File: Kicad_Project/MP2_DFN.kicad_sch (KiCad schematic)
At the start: 228 parts, among them J1 Conn_01x07, J2 Conn_01x06, J3 Conn_01x06, J4 Conn_01x06, SW1 Conn_01x02, U1 NCP5183 / TF2190-TAH, U2 NCP5183 / TF2190-TAH, U3 NCP5183 / TF2190-TAH, U4 NCS20034DR2G, U5 STM32F401CCU6_Balckpill, U6 PQDE6W-Q110 / RD5-110S12W, U7 12_DCDC_5

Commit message: changed all file names
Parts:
- QA1, QA2, QA3, QA4, QA5, QA6, QB1, QB2, QB3, QB4, QB5, QB6, QC1, QC2, QC3, QC4, QC5, QC6: symbol CCC_ESC_Custom_Symbols:MDP10N027 -> MP2_DFN_Custom_Symbols:MDP10N027
- SHA1, SHA2, SHA3, SHB1, SHB2, SHB3, SHC1, SHC2, SHC3: footprint CCC_ESC_Custom_parts:Shunt_2512_6332Metric -> MP2_DFN_Custom_parts:Shunt_2512_6332Metric
- U1, U2, U3: symbol CCC_ESC_Custom_Symbols:NCP5183 -> MP2_DFN_Custom_Symbols:NCP5183
- U5: footprint CCC_ESC_Custom_parts:Blackpill_STM32F401CEU6 -> MP2_DFN_Custom_parts:Blackpill_STM32F401CEU6; symbol CCC_ESC_Custom_Symbols:STM32F401CCU6_Balckpill -> MP2_DFN_Custom_Symbols:STM32F401CCU6_Balckpill
- U6: footprint CCC_ESC_Custom_parts:PQDE6W -> MP2_DFN_Custom_parts:PQDE6W; symbol CCC_ESC_Custom_Symbols:PQDE6W-Q110 -> MP2_DFN_Custom_Symbols:PQDE6W-Q110
- U7: footprint CCC_ESC_Custom_parts:12_DCDC_5 -> MP2_DFN_Custom_parts:12_DCDC_5; symbol CCC_ESC_Custom_Symbols:TO220_replacement_module -> MP2_DFN_Custom_Symbols:TO220_replacement_module

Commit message: created manufacturing files
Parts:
- removed SW1: Conn_01x02, Resistor_SMD:R_1206_3216Metric_Pad1.30x1.75mm_HandSolder, symbol Connector_Generic:Conn_01x02
- CR1, CR2, CR3, CR4, CR5, CS1, CS2, CS3, D10, D8, J1, J2, J3, J4, JP1, JP2, JP3, NT1, NT2, NT3, NT4, NT5, NT6, NTC1, PHA_1, PHA_2, PHB_1, PHB_2, PHC_1, PHC_2, QA1, QA2, QA3, QA4, QA5, QA6, QB1, QB2, QB3, QB4, QB5, QB6, QC1, QC2, QC3, QC4, QC5, QC6, RS1, RS2, RS3, Tp12V1, TpGND1, TpGND2, TpGND3, TpGND4, TpGS2, TpGS4, TpGS6, U5, U6, U7: now left out of the parts list
- R38, R40: value 47k -> 13k; LCSC C25819 -> C22797
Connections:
- net at C5.1, D7.1 (A1), D8.1 (A1)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: now also R1.1, R2.1
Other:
- note added: "R38 and R40 values for Vsense dividers - for different power stage Voltages. Since the we're going with the NVMTSC4D3N15MC MOSFETs, Vsense will be for 150V: 150V max 30s lipo, overvoltage cutoff at 137V) - 13k (LCSC C22797) 100V max 20s lipo, overvoltage cutoff at 92.6V) - 47k (LCSC C25819) 80V max 16s lipo, overvoltage cutoff at 75.6V) - Do not fit at all!"
- note removed: "CAUTION WITH ORDERING -- FIX BOM FOR 150V VSENSE"
- note removed: "R38 and R40 values for Vsense dividers - for different power stage Voltages. 80V power stage (max 16s lipo, overvoltage cutoff at 75.6V) - Do not fit at all! 100V power stage (max 20s lipo, overvoltage cutoff at 92.6V) - 47k (LCSC C25819) 150V power stage (max 30s lipo, overvoltage cutoff at 137V) - 13k (LCSC C22797)"
- moved on the sheet: R1, R2

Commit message: order sent to jlcpcb
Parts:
- U1, U2, U3: value NCP5183 / TF2190-TAH -> TF2190-TAH
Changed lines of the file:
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@@
       (effects (font (size 1.27 1.27)))
     )
-    (property "Value" "NCP5183 / TF2190-TAH" (at 431.165 228.6 0)
+    (property "Value" "TF2190-TAH" (at 431.165 228.6 0)
       (effects (font (size 1.27 1.27)))
     )
@@
       (effects (font (size 1.27 1.27)) hide)
     )
-    (property "Value" "NCP5183 / TF2190-TAH" (at 431.165 67.31 0)
+    (property "Value" "TF2190-TAH" (at 431.165 67.31 0)
       (effects (font (size 1.27 1.27)))
     )
@@
       (effects (font (size 1.27 1.27)))
     )
-    (property "Value" "NCP5183 / TF2190-TAH" (at 431.165 147.32 0)
+    (property "Value" "TF2190-TAH" (at 431.165 147.32 0)
       (effects (font (size 1.27 1.27)))
     )

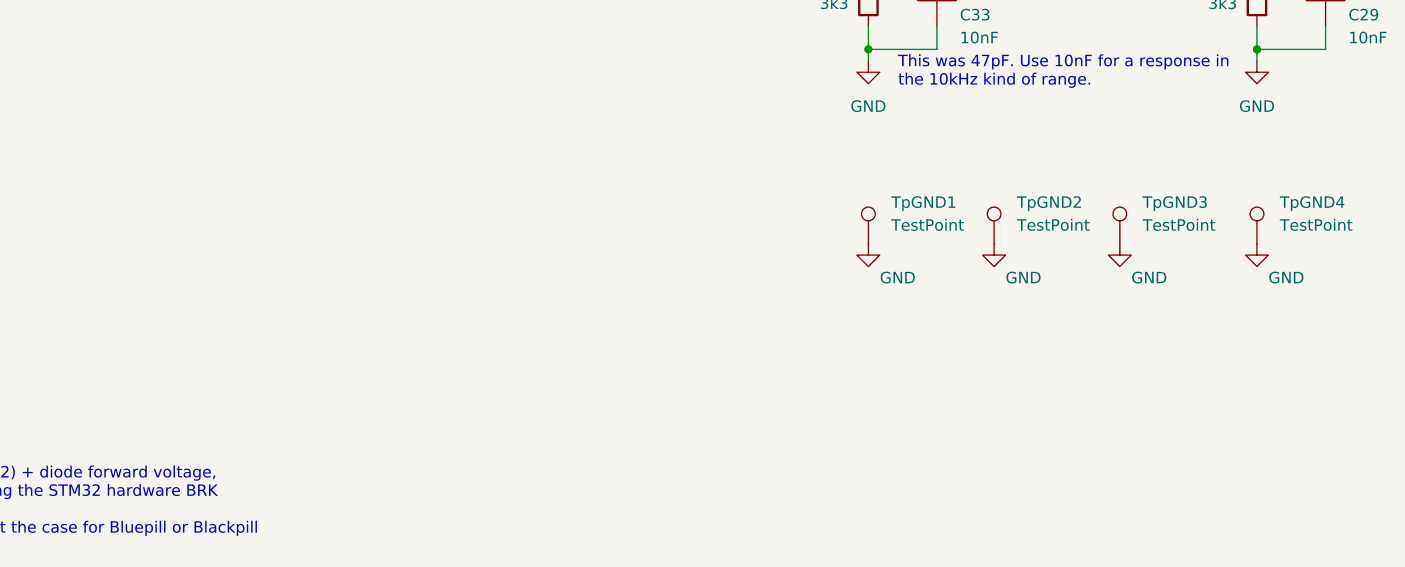
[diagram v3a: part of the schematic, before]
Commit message: fixed GND breaks, increased bus bars
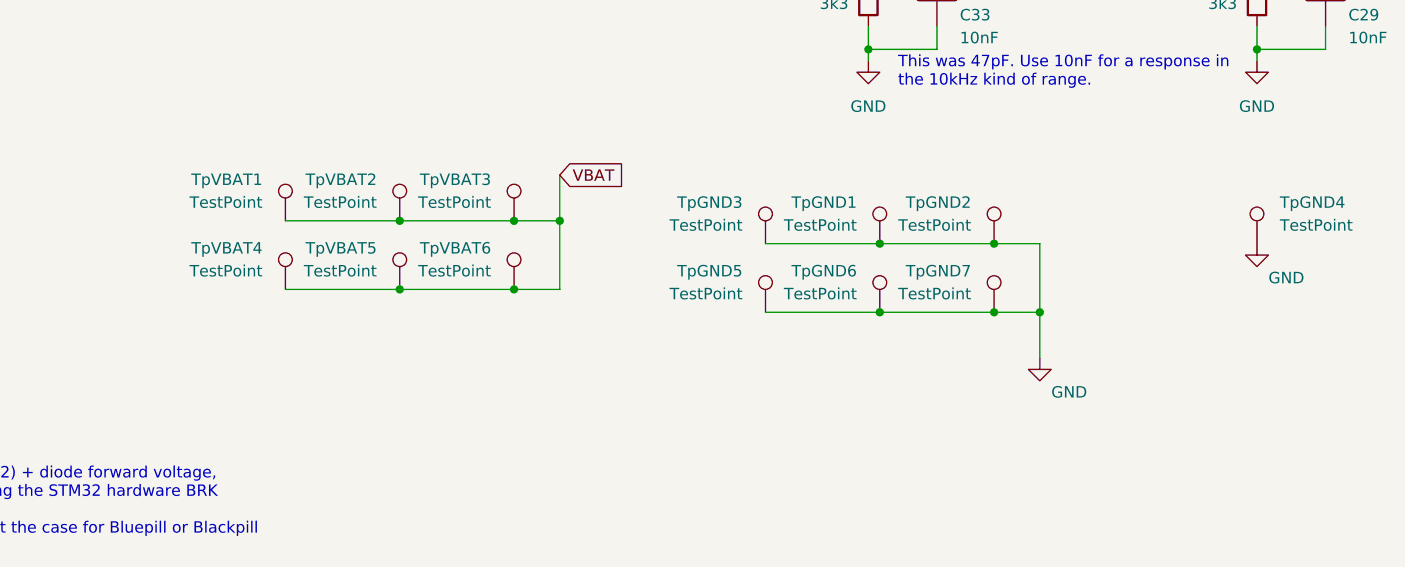
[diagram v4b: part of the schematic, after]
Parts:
- added TpGND5, TpGND6, TpGND7, TpVBAT1, TpVBAT2, TpVBAT3, TpVBAT4, TpVBAT5, TpVBAT6: TestPoint, Busbars:my_testpoint_D1.7mm, symbol Connector:TestPoint
- TpGND1, TpGND2, TpGND3: footprint TestPoint:TestPoint_THTPad_D2.0mm_Drill1.0mm -> Busbars:my_testpoint_D1.7mm
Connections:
- net GND: now also TpGND5.1, TpGND6.1, TpGND7.1
- net VBAT: now also TpVBAT1.1, TpVBAT2.1, TpVBAT3.1, TpVBAT4.1, TpVBAT5.1, TpVBAT6.1
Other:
- moved on the sheet: TpGND3

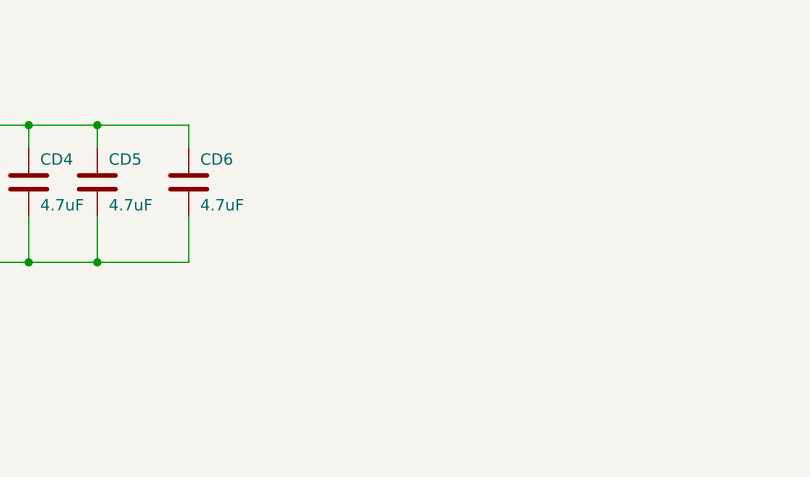
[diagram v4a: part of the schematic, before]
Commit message: added caps, prettied up phase connectors
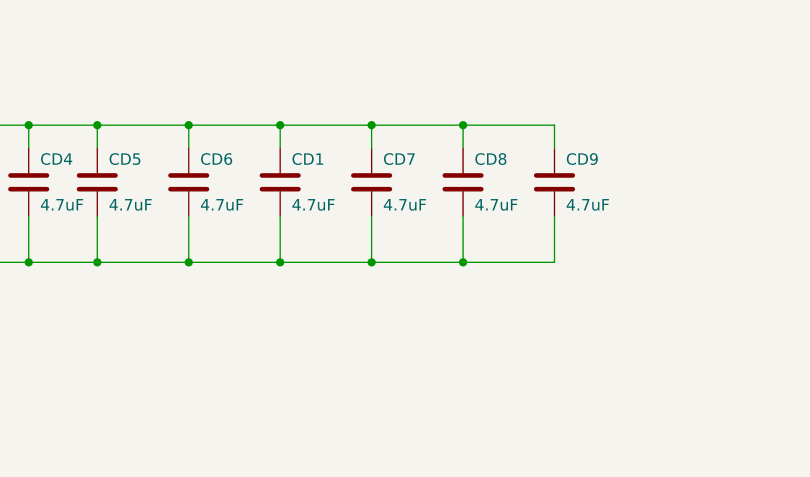
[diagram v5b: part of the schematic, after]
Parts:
- added CD1, CD7, CD8, CD9: 4.7uF, Capacitor_SMD:C_1210_3225Metric, symbol Device:C
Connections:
- net GND: now also CD1.2, CD7.2, CD8.2, CD9.2
- net VBAT: now also CD1.1, CD7.1, CD8.1, CD9.1
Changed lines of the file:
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@@
   (junction (at 486.41 156.21) (diameter 0) (color 0 0 0 0)
   )
+  (junction (at 179.705 43.815) (diameter 0) (color 0 0 0 0)
+  )
   (junction (at 452.755 76.2) (diameter 0) (color 0 0 0 0)
   )
@@
   (junction (at 250.698 380.492) (diameter 0) (color 0 0 0 0)
   )
+  (junction (at 149.225 43.815) (diameter 0) (color 0 0 0 0)
+  )
   (junction (at 448.31 241.3) (diameter 0) (color 0 0 0 0)
   )
@@
   (junction (at 491.49 328.93) (diameter 0) (color 0 0 0 0)
   )
+  (junction (at 159.385 43.815) (diameter 0) (color 0 0 0 0)
+  )
   (junction (at 534.67 241.3) (diameter 0) (color 0 0 0 0)
   )
@@
   (junction (at 443.23 59.69) (diameter 0) (color 0 0 0 0)
   )
+  (junction (at 179.705 28.575) (diameter 0) (color 0 0 0 0)
+  )
   (junction (at 538.48 80.01) (diameter 0) (color 0 0 0 0)
   )
@@
   (junction (at 246.38 46.99) (diameter 0) (color 0 0 0 0)
   )
+  (junction (at 169.545 43.815) (diameter 0) (color 0 0 0 0)
+  )
   (junction (at 451.485 241.3) (diameter 0) (color 0 0 0 0)
   )
@@
   (junction (at 466.725 229.87) (diameter 0) (color 0 0 0 0)
   )
+  (junction (at 169.545 28.575) (diameter 0) (color 0 0 0 0)
+  )
   (junction (at 474.98 180.975) (diameter 0) (color 0 0 0 0)
   )
@@
   (junction (at 526.415 229.87) (diameter 0) (color 0 0 0 0)
   )
+  (junction (at 149.225 28.575) (diameter 0) (color 0 0 0 0)
+  )
   (junction (at 419.1 256.54) (diameter 0) (color 0 0 0 0)
   )
@@
   (junction (at 140.97 133.35) (diameter 0) (color 0 0 0 0)
   )
+  (junction (at 159.385 28.575) (diameter 0) (color 0 0 0 0)
+  )
   (junction (at 406.4 360.68) (diameter 0) (color 0 0 0 0)
   )
@@
     (stroke (width 0) (type default))
   )
+  (wire (pts (xy 149.225 43.815) (xy 159.385 43.815))
+    (stroke (width 0) (type default))
+  )
   (wire (pts (xy 487.68 160.02) (xy 504.19 160.02))
     (stroke (width 0) (type default))
@@
     (stroke (width 0) (type default))
   )
+  (wire (pts (xy 159.385 43.815) (xy 169.545 43.815))
+    (stroke (width 0) (type default))
+  )
+  (wire (pts (xy 159.385 28.575) (xy 159.385 31.115))
+    (stroke (width 0) (type default))
+  )
   (wire (pts (xy 458.47 72.39) (xy 458.47 80.01))
     (stroke (width 0) (type default))
@@
     (stroke (width 0) (type default))
   )
+  (wire (pts (xy 179.705 43.815) (xy 189.865 43.815))
+    (stroke (width 0) (type default))
+  )
   (wire (pts (xy 86.36 63.5) (xy 86.36 67.31))
     (stroke (width 0) (type default))
@@
     (stroke (width 0) (type default))
   )
+  (wire (pts (xy 179.705 38.735) (xy 179.705 43.815))
+    (stroke (width 0) (type default))
+  )
   (wire (pts (xy 243.84 33.02) (xy 246.38 33.02))
     (stroke (width 0) (type default))
@@
     (stroke (width 0) (type default))
   )
+  (wire (pts (xy 179.705 28.575) (xy 189.865 28.575))
+    (stroke (width 0) (type default))
+  )
   (wire (pts (xy 104.14 241.3) (xy 110.49 241.3))
     (stroke (width 0) (type default))
@@
     (stroke (width 0) (type default))
   )
+  (wire (pts (xy 169.545 43.815) (xy 179.705 43.815))
+    (stroke (width 0) (type default))
+  )
   (wire (pts (xy 466.09 148.59) (xy 466.725 148.59))
     (stroke (width 0) (type default))
@@
     (stroke (width 0) (type default))
   )
+  (wire (pts (xy 189.865 38.735) (xy 189.865 43.815))
+    (stroke (width 0) (type default))
+  )
   (wire (pts (xy 448.31 160.02) (xy 448.31 176.53))
     (stroke (width 0) (type default))
@@
     (stroke (width 0) (type default))
   )
+  (wire (pts (xy 169.545 28.575) (xy 169.545 31.115))
+    (stroke (width 0) (type default))
+  )
   (wire (pts (xy 60.96 119.38) (xy 60.96 121.92))
     (stroke (width 0) (type default))
@@
     (stroke (width 0) (type default))
   )
+  (wire (pts (xy 179.705 28.575) (xy 179.705 31.115))
+    (stroke (width 0) (type default))
+  )
   (wire (pts (xy 504.19 140.97) (xy 504.19 143.51))
     (stroke (width 0) (type default))
@@
     (stroke (width 0) (type default))
   )
+  (wire (pts (xy 159.385 28.575) (xy 169.545 28.575))
+    (stroke (width 0) (type default))
+  )
   (wire (pts (xy 518.795 152.4) (xy 518.16 152.4))
     (stroke (width 0) (type default))
@@
     (stroke (width 0) (type default))
   )
+  (wire (pts (xy 149.225 28.575) (xy 159.385 28.575))
+    (stroke (width 0) (type default))
+  )
   (wire (pts (xy 156.718 141.732) (xy 156.718 144.272))
     (stroke (width 0) (type default))
@@
     (stroke (width 0) (type default))
   )
+  (wire (pts (xy 169.545 28.575) (xy 179.705 28.575))
+    (stroke (width 0) (type default))
+  )
   (wire (pts (xy 199.39 87.63) (xy 204.47 87.63))
     (stroke (width 0) (type default))
@@
     (stroke (width 0) (type default))
   )
+  (wire (pts (xy 189.865 28.575) (xy 189.865 31.115))
+    (stroke (width 0) (type default))
+  )
   (wire (pts (xy 440.69 314.96) (xy 440.69 318.77))
     (stroke (width 0) (type default))
@@
     (stroke (width 0) (type default))
   )
+  (wire (pts (xy 159.385 38.735) (xy 159.385 43.815))
+    (stroke (width 0) (type default))
+  )
   (wire (pts (xy 274.828 320.802) (xy 277.368 320.802))
     (stroke (width 0) (type default))
@@
     (stroke (width 0) (type default))
   )
+  (wire (pts (xy 169.545 38.735) (xy 169.545 43.815))
+    (stroke (width 0) (type default))
+  )
   (wire (pts (xy 220.472 199.898) (xy 220.472 201.168))
     (stroke (width 0) (type default))
@@
     )
   )
+  (symbol (lib_id "Device:C") (at 189.865 34.925 0) (unit 1)
+    (in_bom yes) (on_board yes) (dnp no)
+    (property "Reference" "CD9" (at 191.135 32.385 0)
+      (effects (font (size 1.27 1.27)) (justify left))
+    )
+    (property "Value" "4.7uF" (at 191.135 37.465 0)
+      (effects (font (size 1.27 1.27)) (justify left))
+    )
+    (property "Footprint" "Capacitor_SMD:C_1210_3225Metric" (at 190.8302 38.735 0)
+      (effects (font (size 1.27 1.27)) hide)
+    )
+    (property "Datasheet" "~" (at 189.865 34.925 0)
+      (effects (font (size 1.27 1.27)) hide)
+    )
+    (property "MFR PT" "FS32X475K101EGG" (at 189.865 34.925 0)
+      (effects (font (size 1.27 1.27)) hide)
+    )
+    (property "LCSC" "C381466" (at 189.865 34.925 0)
+      (effects (font (size 1.27 1.27)) hide)
+    )
+    (pin "1")
+    (pin "2")
+    (instances
+      (project "MP2_DFN"
+        (path "/31a3399e-b0e0-4a61-aacb-f319bb9df4d3"
+          (reference "CD9") (unit 1)
+        )
+      )
+    )
+  )
   (symbol (lib_id "Device:R") (at 534.67 185.42 180) (unit 1)
     (in_bom yes) (on_board yes) (dnp no)
@@
     )
   )
+  (symbol (lib_id "Device:C") (at 179.705 34.925 0) (unit 1)
+    (in_bom yes) (on_board yes) (dnp no)
+    (property "Reference" "CD8" (at 180.975 32.385 0)
+      (effects (font (size 1.27 1.27)) (justify left))
+    )
+    (property "Value" "4.7uF" (at 180.975 37.465 0)
+      (effects (font (size 1.27 1.27)) (justify left))
+    )
+    (property "Footprint" "Capacitor_SMD:C_1210_3225Metric" (at 180.6702 38.735 0)
+      (effects (font (size 1.27 1.27)) hide)
+    )
+    (property "Datasheet" "~" (at 179.705 34.925 0)
+      (effects (font (size 1.27 1.27)) hide)
+    )
+    (property "MFR PT" "FS32X475K101EGG" (at 179.705 34.925 0)
+      (effects (font (size 1.27 1.27)) hide)
+    )
+    (property "LCSC" "C381466" (at 179.705 34.925 0)
+      (effects (font (size 1.27 1.27)) hide)
+    )
+    (pin "1")
+    (pin "2")
+    (instances
+      (project "MP2_DFN"
+        (path "/31a3399e-b0e0-4a61-aacb-f319bb9df4d3"
+          (reference "CD8") (unit 1)
+        )
+      )
+    )
+  )
   (symbol (lib_id "Device:R") (at 448.31 261.62 180) (unit 1)
     (in_bom no) (on_board yes) (dnp no)
@@
     )
   )
+  (symbol (lib_id "Device:C") (at 169.545 34.925 0) (unit 1)
+    (in_bom yes) (on_board yes) (dnp no)
+    (property "Reference" "CD7" (at 170.815 32.385 0)
+      (effects (font (size 1.27 1.27)) (justify left))
+    )
+    (property "Value" "4.7uF" (at 170.815 37.465 0)
+      (effects (font (size 1.27 1.27)) (justify left))
+    )
+    (property "Footprint" "Capacitor_SMD:C_1210_3225Metric" (at 170.5102 38.735 0)
+      (effects (font (size 1.27 1.27)) hide)
+    )
+    (property "Datasheet" "~" (at 169.545 34.925 0)
+      (effects (font (size 1.27 1.27)) hide)
+    )
+    (property "MFR PT" "FS32X475K101EGG" (at 169.545 34.925 0)
+      (effects (font (size 1.27 1.27)) hide)
+    )
+    (property "LCSC" "C381466" (at 169.545 34.925 0)
+      (effects (font (size 1.27 1.27)) hide)
+    )
+    (pin "1")
+    (pin "2")
+    (instances
+      (project "MP2_DFN"
+        (path "/31a3399e-b0e0-4a61-aacb-f319bb9df4d3"
+          (reference "CD7") (unit 1)
+        )
+      )
+    )
+  )
   (symbol (lib_id "Device:R") (at 534.67 105.41 180) (unit 1)
     (in_bom yes) (on_board yes) (dnp no)
@@
         )
       )
+    )
+  )
+  (symbol (lib_id "Device:C") (at 159.385 34.925 0) (unit 1)
+    (in_bom yes) (on_board yes) (dnp no)
+    (property "Reference" "CD1" (at 160.655 32.385 0)
+      (effects (font (size 1.27 1.27)) (justify left))
+    )
+    (property "Value" "4.7uF" (at 160.655 37.465 0)
+      (effects (font (size 1.27 1.27)) (justify left))
+    )
+    (property "Footprint" "Capacitor_SMD:C_1210_3225Metric" (at 160.3502 38.735 0)
+      (effects (font (size 1.27 1.27)) hide)
+    )
+    (property "Datasheet" "~" (at 159.385 34.925 0)
+      (effects (font (size 1.27 1.27)) hide)
+    )
+    (property "MFR PT" "FS32X475K101EGG" (at 159.385 34.925 0)
+      (effects (font (size 1.27 1.27)) hide)
+    )
+    (property "LCSC" "C381466" (at 159.385 34.925 0)
+      (effects (font (size 1.27 1.27)) hide)
+    )
+    (pin "1")
+    (pin "2")
+    (instances
+      (project "MP2_DFN"
+        (path "/31a3399e-b0e0-4a61-aacb-f319bb9df4d3"
+          (reference "CD1") (unit 1)
+        )
+      )
